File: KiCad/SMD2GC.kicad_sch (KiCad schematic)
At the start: 3 parts, among them J1 Conn_01x06, J2 DE9_Plug

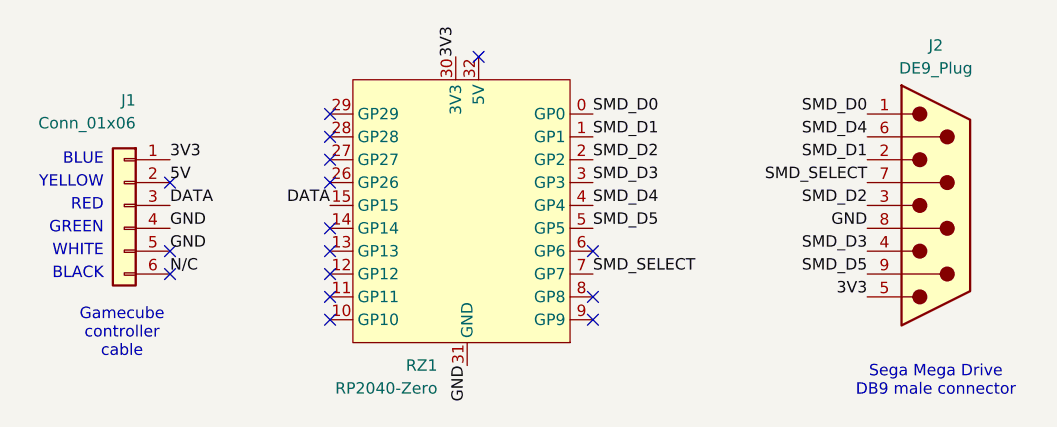
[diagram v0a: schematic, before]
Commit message: Update schematic for USB VBUS +5V power from GameCube rumble power.
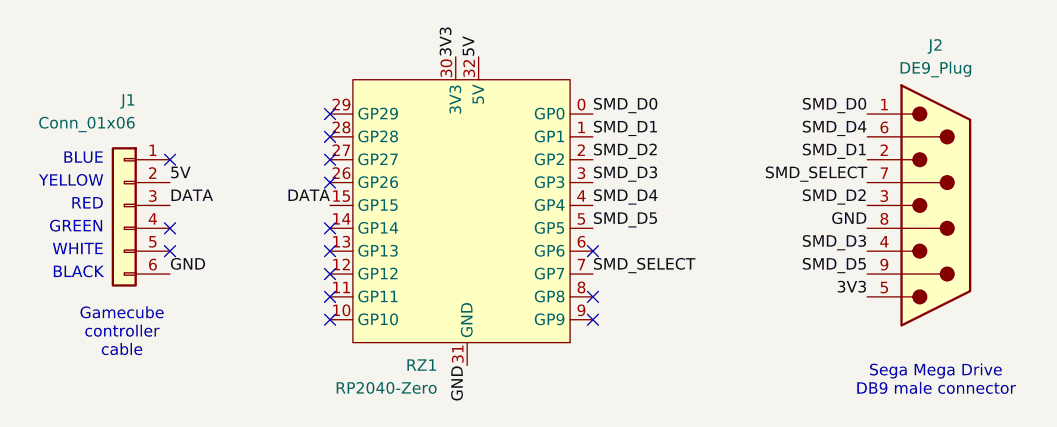
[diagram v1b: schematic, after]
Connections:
- net N/C is gone; now on net GND: J1.6 (Pin_6)
- net 3V3: no longer J1.1 (Pin_1)
- net 5V: now also RZ1.32 (5V)
- net GND: no longer J1.4 (Pin_4), J1.5 (Pin_5)
- no-connect marks 16 -> 15
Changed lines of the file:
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@@
-	)
-	(no_connect
-		(at 36.83 43.18)
-	)
-	(no_connect
-		(at 36.83 53.34)
 	)
 	(no_connect
@@
 	)
 	(no_connect
+		(at 36.83 40.64)
+	)
+	(no_connect
 		(at 54.61 55.88)
 	)
@@
 	)
 	(no_connect
+		(at 36.83 48.26)
+	)
+	(no_connect
 		(at 54.61 35.56)
 	)
@@
 	)
 	(no_connect
-		(at 71.12 29.21)
-	)
-	(no_connect
 		(at 83.82 50.8)
 	)
@@
 			)
 			(justify right)
-		)
-	)
-	(label "GND"
-		(at 36.83 48.26 0)
-		(fields_autoplaced yes)
-		(effects
-			(font
-				(size 1.27 1.27)
-			)
-			(justify left bottom)
 		)
 	)
@@
 	)
 	(label "GND"
-		(at 36.83 50.8 0)
+		(at 36.83 53.34 0)
 		(fields_autoplaced yes)
 		(effects
@@
 		)
 	)
-	(label "3V3"
-		(at 36.83 40.64 0)
-		(fields_autoplaced yes)
-		(effects
-			(font
-				(size 1.27 1.27)
-			)
-			(justify left bottom)
-		)
-	)
 	(label "SMD_D4"
 		(at 83.82 45.72 0)
@@
 		)
 	)
-	(label "N{slash}C"
-		(at 36.83 53.34 0)
-		(fields_autoplaced yes)
-		(effects
-			(font
-				(size 1.27 1.27)
-			)
-			(justify left bottom)
-		)
-	)
 	(label "5V"
 		(at 36.83 43.18 0)
@@
 		)
 	)
+	(label "5V"
+		(at 71.12 29.21 90)
+		(fields_autoplaced yes)
+		(effects
+			(font
+				(size 1.27 1.27)
+			)
+			(justify left bottom)
+		)
+	)
